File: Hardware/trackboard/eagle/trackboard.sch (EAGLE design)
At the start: 29 parts, among them U9.00 ADNS-3080, U9.02 SI1922EDH, X9.00 RESON

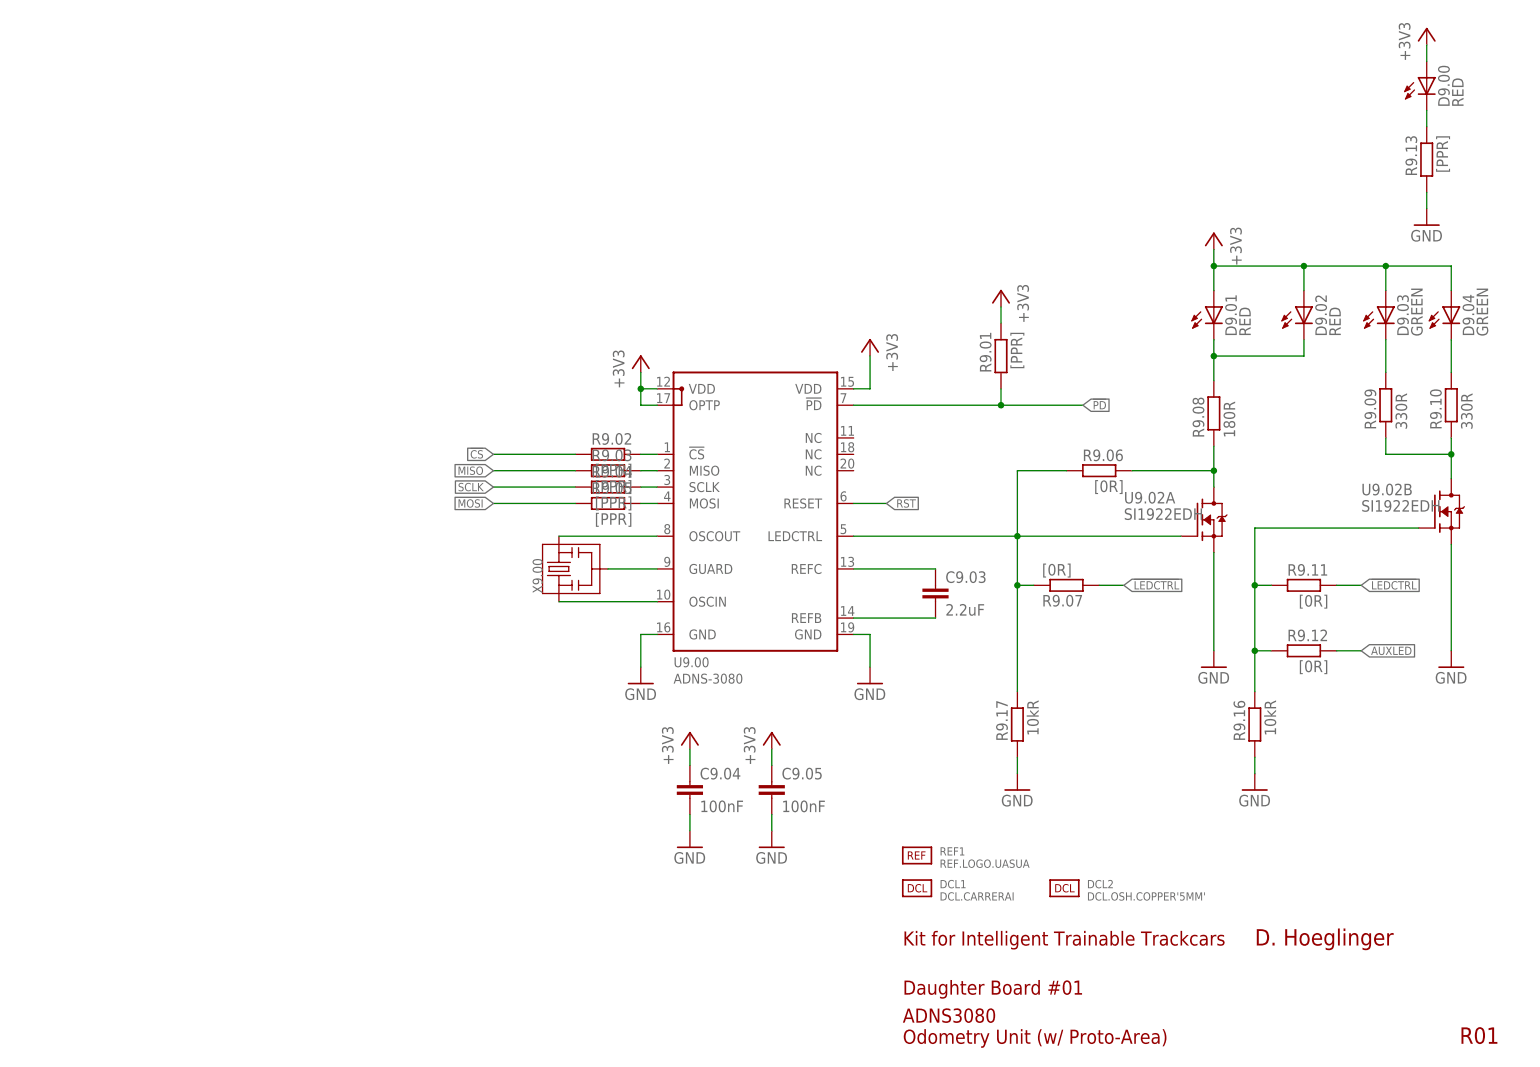
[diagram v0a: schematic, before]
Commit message: board dimensions fixed ; layed out some traces ; needs clarification on what's allowed regarding cuts through pads
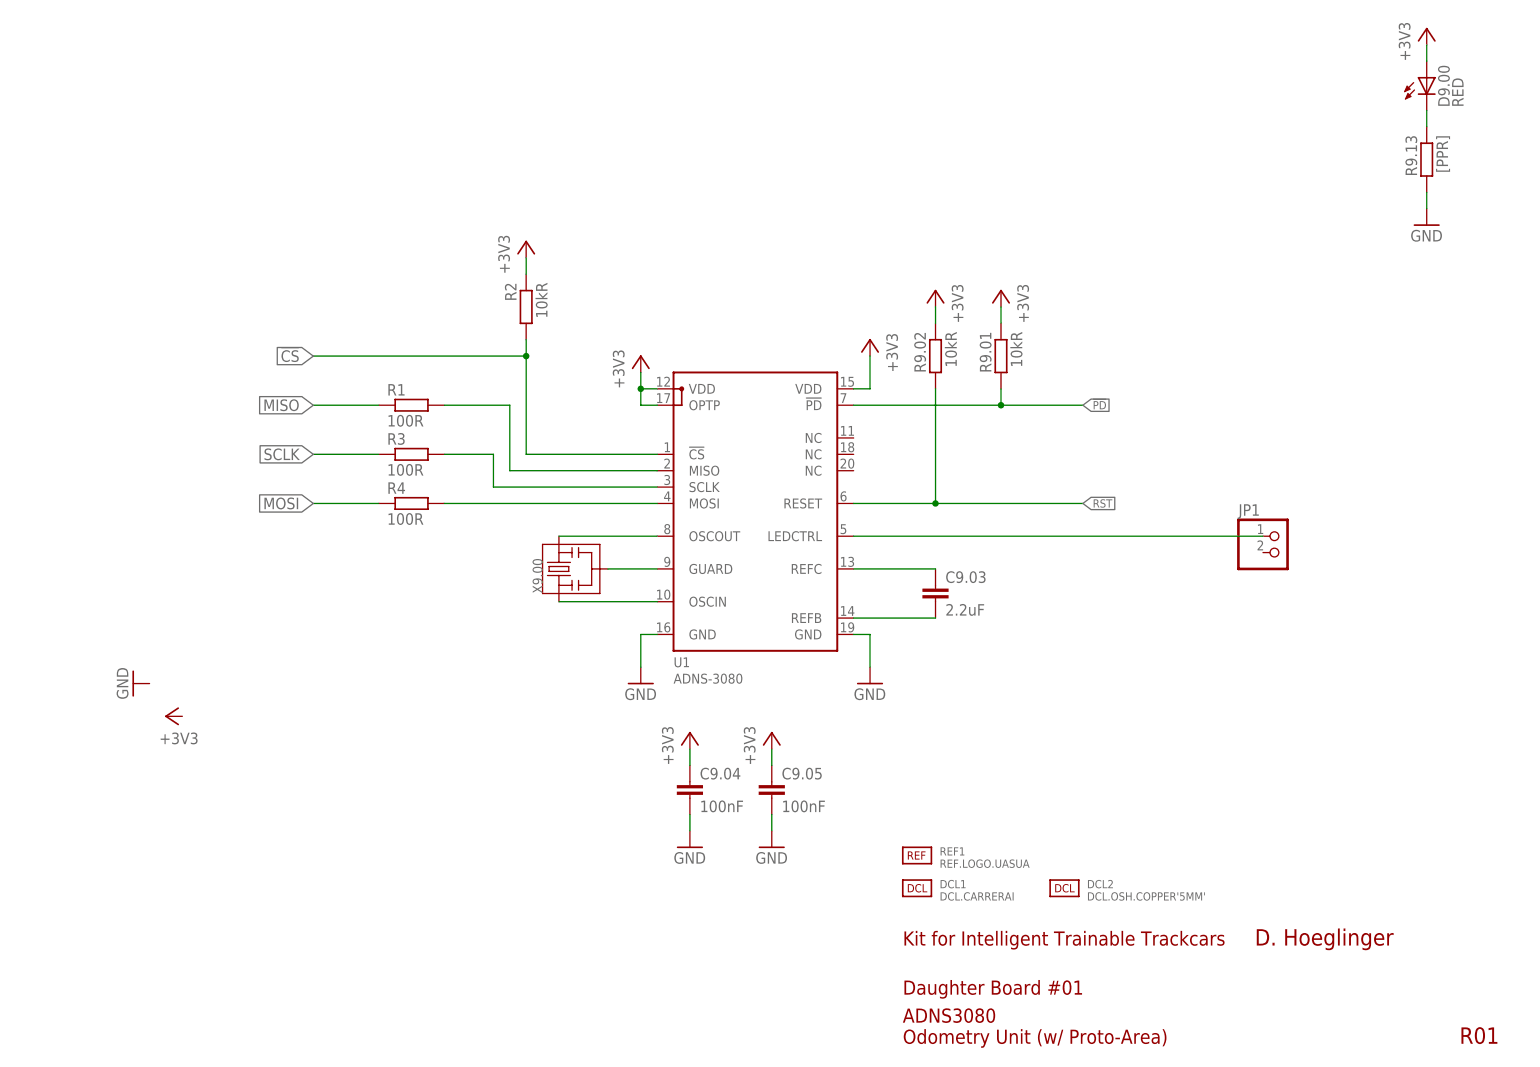
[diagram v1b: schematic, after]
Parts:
- removed D9.01: RED, led:LED5MM
- removed D9.02: RED, led:LEDCHIP-LED0805
- removed D9.03, D9.04: GREEN, led:LEDCHIP-LED0805
- removed R9.03, R9.04, R9.05: [PPR], rcl:R-EU_R0805
- removed R9.06, R9.07, R9.11, R9.12: [0R], rcl:R-EU_R0805
- removed R9.08: 180R, rcl:R-EU_R0805
- removed R9.09, R9.10: 330R, rcl:R-EU_R0805
- removed R9.16, R9.17: 10kR, rcl:R-EU_R0805
- removed U9.02: SI1922EDH, kitt.ic:SI1922EDH
- added JP1: (no value), pinhead:PINHD-1X2
- added R1, R3, R4: 100R, rcl:R-EU_R0402
- added R2: 10kR, rcl:R-EU_R0402
- R9.01, R9.02: value [PPR] -> 10kR; device rcl:R-EU_R0805 -> rcl:R-EU_R0402
- renumbered U9.00 to U1
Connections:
- removed net !LEDCTRL: R9.07.2, R9.11.1
- removed net AUXLED: R9.12.1
- removed net N$168: R9.02.1, U1.!CS
- removed net N$182: R9.03.1, U1.MISO
- removed net N$183: R9.04.1, U1.SCLK
- removed net N$184: R9.11.2, R9.12.2, R9.16.1, U9.02B.G
- removed net N$185: D9.04.C, R9.10.2
- removed net N$186: R9.09.1, R9.10.1, U9.02B.D
- removed net N$187: D9.03.C, R9.09.2
- removed net N$188: R9.05.1, U1.MOSI
- removed net N$4: R9.06.2, R9.07.1, R9.17.1, U1.LEDCTRL, U9.02A.G
- removed net N$8: D9.01.C, D9.02.C, R9.08.2
- new net U1.MISO: R1.2, U1.MISO
- new net U1.MOSI: R4.2, U1.MOSI
- new net U1.SCLK: R3.2, U1.SCLK
- net !CS: now also R2.2, U1.!CS; no longer R9.02.2
- net +3V3: now also R2.1, R9.02.1; no longer D9.01.A, D9.02.A, D9.03.A, D9.04.A
- net GND: no longer R9.16.2, R9.17.2, U9.02A.S, U9.02B.S
- net MISO: now also R1.1; no longer R9.03.2
- net MOSI: now also R4.1; no longer R9.05.2
- net N$7: now also JP1.1, U1.LEDCTRL; no longer R9.06.1, R9.08.1, U9.02A.D
- net RST: now also R9.02.2
- net SCLK: now also R3.1; no longer R9.04.2
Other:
- moved on the sheet: R9.02

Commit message: ADNS3080 module is pretty much okay now ; will be imported into correct place in baseboard
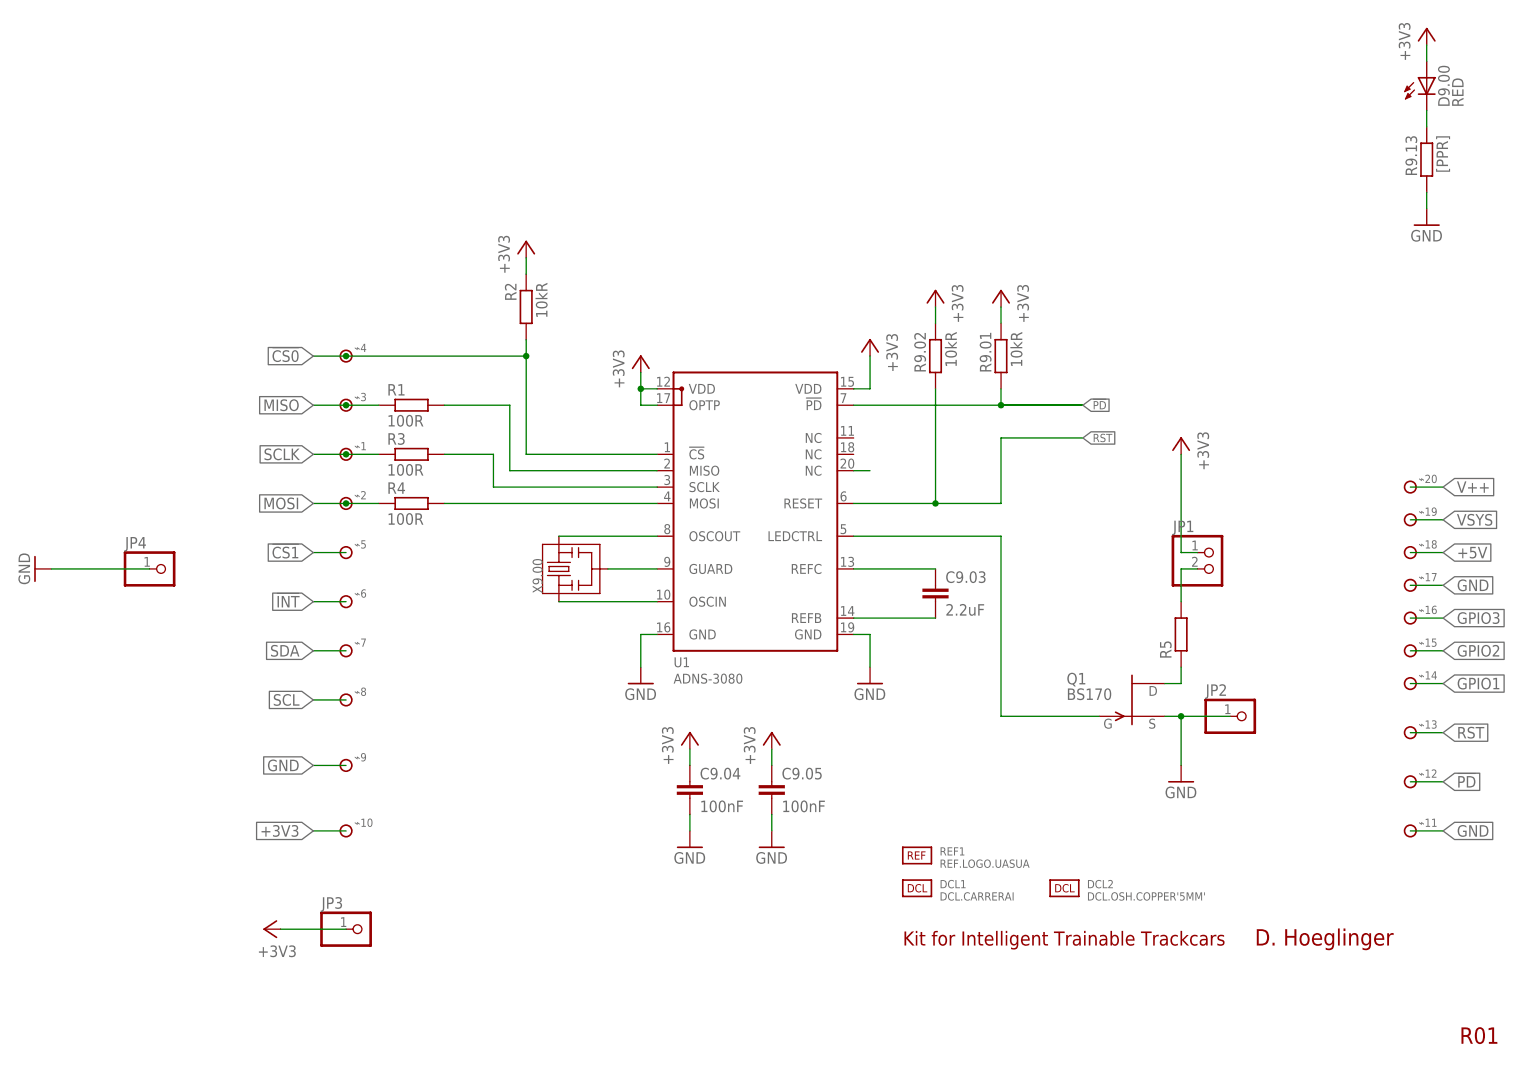
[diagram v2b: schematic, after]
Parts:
- added JP2, JP3, JP4: (no value), pinhead:PINHD-1X1
- added Q1: BS170, transistor-fet:SST5484
- added R5: (no value), rcl:R-EU_R0805
- added ⌁1, ⌁10, ⌁11, ⌁12, ⌁13, ⌁14, ⌁15, ⌁16, ⌁17, ⌁18, ⌁19, ⌁2, ⌁20, ⌁3, ⌁4, ⌁5, ⌁6, ⌁7, ⌁8, ⌁9: SINGLEPAD40MIL, kitt.con:SINGLEPAD40MIL
- R9.13: device rcl:R-EU_R0805 -> rcl:R-EU_R0402
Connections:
- removed net !CS: R2.2, U1.!CS
- new net !CS0: R2.2, U1.!CS, ⌁4.P$1
- new net !CS1: ⌁5.P$1
- new net !INT: ⌁6.P$1
- new net GPIO1: ⌁14.P$1
- new net GPIO2: ⌁15.P$1
- new net GPIO3: ⌁16.P$1
- new net N$4: Q1.G, U1.LEDCTRL
- new net N$8: JP1.2, R5.2
- new net N$9: U1.NC@3
- new net SCL: ⌁8.P$1
- new net SDA: ⌁7.P$1
- new net V++: ⌁20.P$1
- net !PD: now also ⌁12.P$1
- net +3V3: now also JP1.1, JP3.1, ⌁10.P$1
- net GND: now also JP2.1, JP4.1, Q1.S, ⌁11.P$1, ⌁17.P$1, ⌁9.P$1
- net MISO: now also ⌁3.P$1
- net MOSI: now also ⌁2.P$1
- net N$7: now also Q1.D, R5.1; no longer JP1.1, U1.LEDCTRL
- net RST: now also ⌁13.P$1
- net SCLK: now also ⌁1.P$1
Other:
- note added: "Odometry Core"
- note added: "[NOTE] MISO/MOSI IS A CROSS CONNECTION"
- note added: "[TODO] PACK AS MODULE FOR EASY IMPORT INTO BASEBOARD"
- note added: "[TODO] REVIEW"
- note added: "[TODO] SILKSCREENING"
- note removed: "ADNS3080 Odometry Unit (w/ Proto-Area)"
- note removed: "Daughter Board #01"
- note removed: "todo: clean up"
- moved on the sheet: JP1
